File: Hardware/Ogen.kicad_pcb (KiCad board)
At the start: 2 copper layers, 22 x 28 mm, 19 parts, among them J1 Input, U1 TLV70019, U2 PMW3360DM-T2QU, U3 SN74LVC1T45DCK, U4 SN74LVC1T45DCK, U5 SN74LVC1T45DCK, U6 SN74LVC1T45DCK, U7 SN74LVC1T45DCK

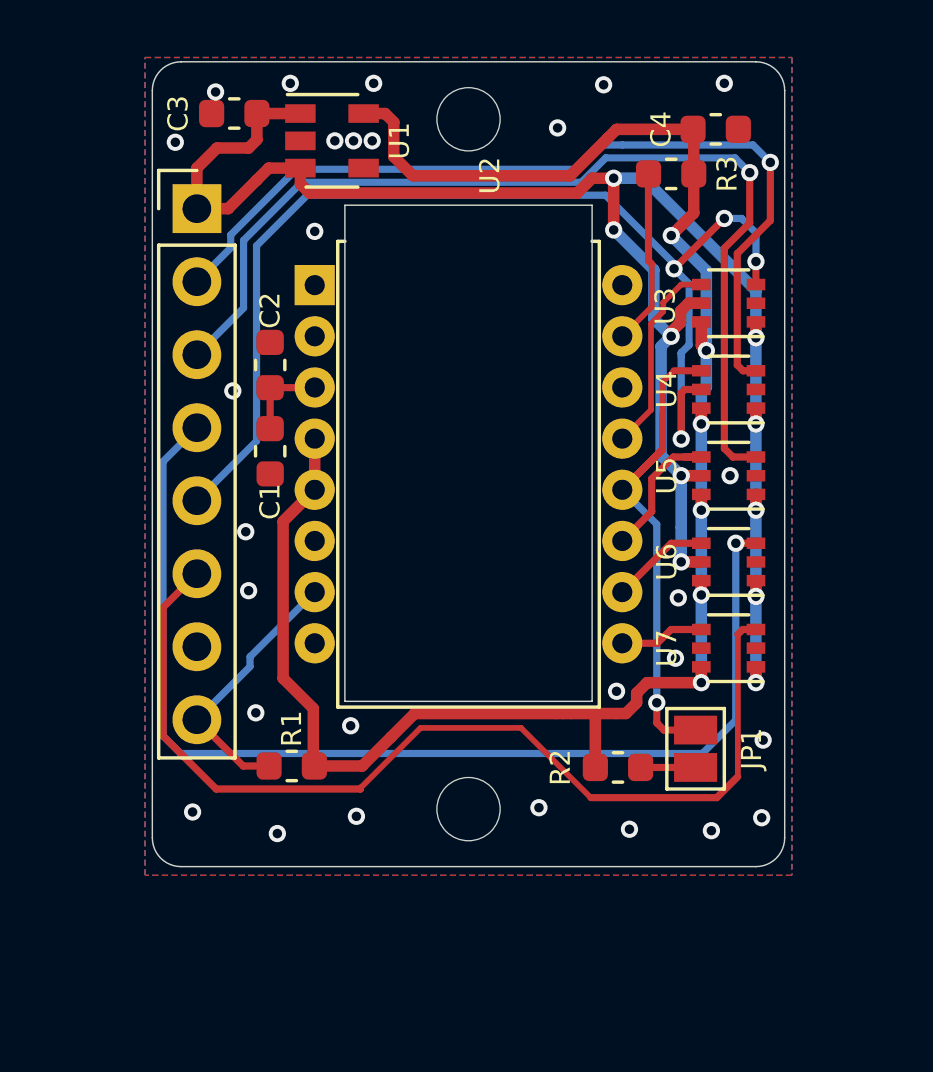
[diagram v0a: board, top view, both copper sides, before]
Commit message: Fixed traces
Some traces weren't the right width so I fixed that. ALso did some minor rerouting.
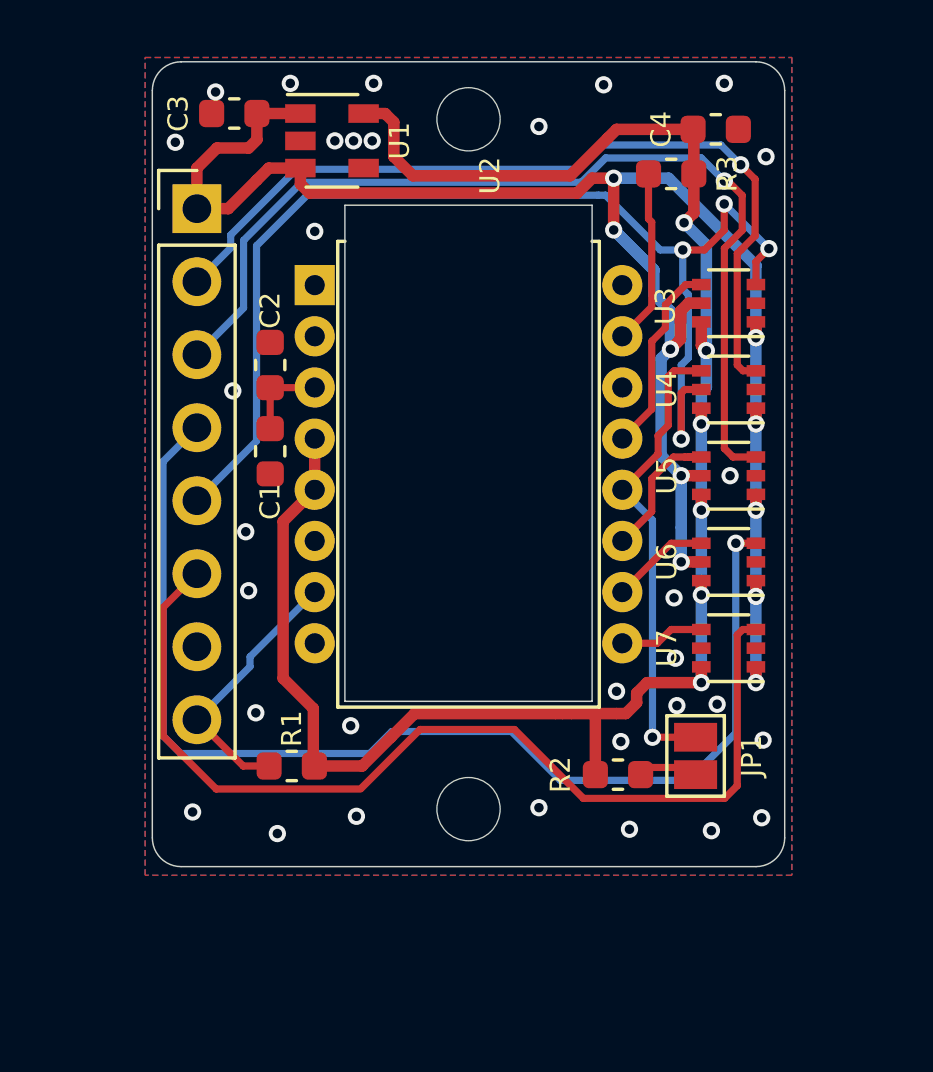
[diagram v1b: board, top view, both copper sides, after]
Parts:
- moved JP1 0.25 mm to (42.9, 35.1)
- moved R2 0.25 mm to (40.2, 35.8)
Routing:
- net VCC: track 63.1 -> 66.5 mm
- net MISO: track 19.1 -> 16.4 mm
- net SCLK-H: track 38.7 -> 40.4 mm
- net MISO-H: track 30.7 -> 29.6 mm
- net SS-H: track 40.5 -> 41.5 mm
- net MOSI-H: track 34.8 -> 34.0 mm
- net GND: vias 28 -> 32

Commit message: Added images and updated readme
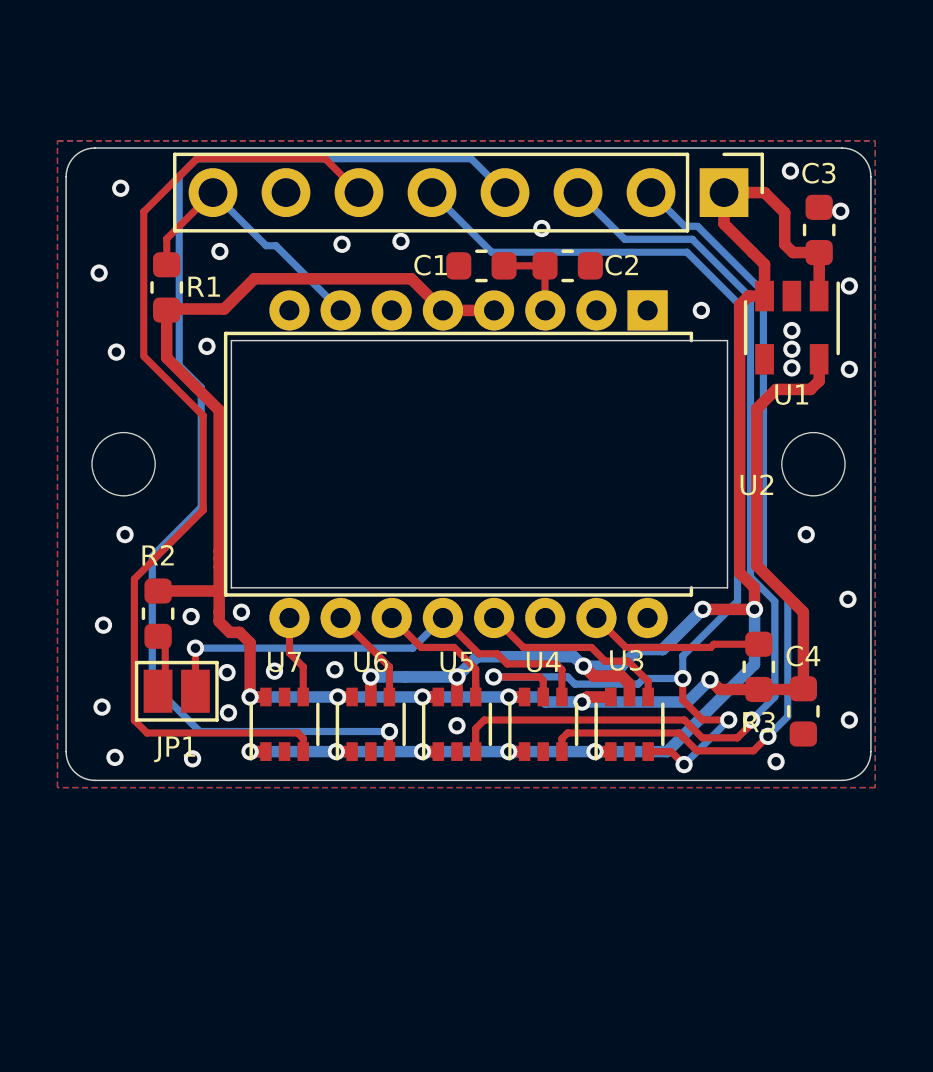
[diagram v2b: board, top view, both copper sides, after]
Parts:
- moved C3 20.7 mm to (47.2, 16.9), turned to 90 degrees
- moved C4 20.5 mm to (46.6, 33.6), turned to 270 degrees
- moved JP1 18.2 mm to (24.9, 32.9), turned to 0 degrees
- moved G*** 17.8 mm to (24.1, 31.2), turned to 180 degrees
- moved R3 17.4 mm to (45.1, 32.0), turned to 90 degrees
- moved U1 17.3 mm to (46.2, 20.2), turned to 270 degrees
- moved R1 17.2 mm to (24.5, 18.9), turned to 270 degrees
- moved REF** 17.0 mm to (47.0, 25.0), turned to 270 degrees
- moved REF** 17.0 mm to (23.0, 25.0), turned to 270 degrees
- moved R2 17.0 mm to (24.2, 30.2), turned to 90 degrees
- moved U7 15.7 mm to (28.6, 34.0), turned to 90 degrees
- moved U3 15.1 mm to (40.6, 34.0), turned to 90 degrees
- moved U6 13.7 mm to (31.6, 34.0), turned to 90 degrees
- moved J1 13.4 mm to (35.0, 15.6), turned to 270 degrees
- moved U4 13.3 mm to (37.6, 34.0), turned to 90 degrees
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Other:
- board size 22 x 28 mm -> 28 x 22 mm

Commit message: Fixed major flaw in PMW3360 footprint
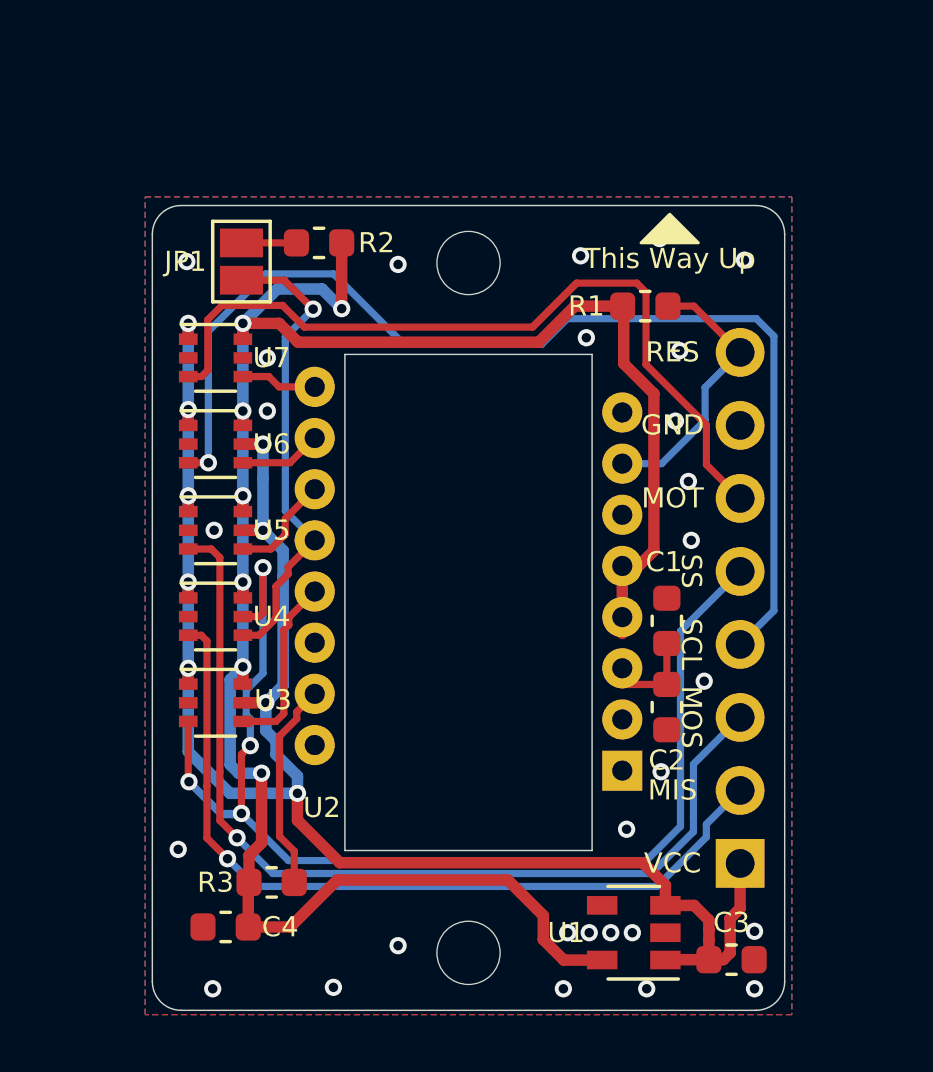
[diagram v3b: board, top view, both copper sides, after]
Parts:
- moved C3 25.6 mm to (44.2, 42.2), turned to 0 degrees
- moved U1 21.8 mm to (40.8, 41.3), turned to 180 degrees
- moved C4 21.5 mm to (26.6, 41.1), turned to 180 degrees
- moved REF** 20.8 mm to (35.0, 42.0), turned to 180 degrees
- moved R3 18.5 mm to (28.1, 39.6), turned to 0 degrees
- moved J1 17.3 mm to (44.5, 30.0), turned to 180 degrees
- moved R1 16.7 mm to (41.1, 19.5), turned to 180 degrees
- moved C2 15.7 mm to (41.9, 33.5), turned to 270 degrees
- moved JP1 15.1 mm to (27.1, 18.0), turned to 270 degrees
- moved U3 14.4 mm to (26.2, 33.3), turned to 0 degrees
- moved R2 14.1 mm to (29.8, 17.3), turned to 0 degrees
- moved C1 13.9 mm to (41.9, 30.4), turned to 90 degrees
- moved REF** 13.9 mm to (35.0, 18.0), turned to 180 degrees
- moved U7 13.0 mm to (26.2, 21.3), turned to 0 degrees
- moved U4 12.0 mm to (26.2, 30.3), turned to 0 degrees
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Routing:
- net VDD: track 65.8 -> 72.5 mm, vias 6 -> 7
- net MOT-H: track 34.8 -> 29.7 mm
- net VCC: track 66.5 -> 61.5 mm, vias 10 -> 9
- net SS-H: track 41.5 -> 44.0 mm
- net SCLK-H: track 40.4 -> 38.6 mm
- net MOSI-H: track 34.0 -> 32.9 mm
- net MISO-H: track 29.6 -> 28.5 mm
- net Net-(R3-Pad2): track 6.17 -> 7.28 mm
- net MOSI: track 5.09 -> 4.26 mm
- net MISO: track 16.4 -> 17.0 mm
- net SCLK: track 3.45 -> 2.86 mm
- net SS: track 6.82 -> 6.23 mm
- net GND: vias 32 -> 28
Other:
- board size 28 x 22 mm -> 22 x 28 mm
- board text added: "GND"
- board text added: "MIS"
- board text added: "MOS"
- board text added: "MOT"
- board text added: "Ogen PMW3360DM-T2QU SPI Breakout Board V1.0 Designed by Aria"
- board text added: "RES"
- board text added: "SCL"
- board text added: "SS"
- board text added: "This Way Up"
- board text added: "VCC"
- board text removed: "Ogen PMW3360 SPI Breakout Board V1.0 Designed by Aria"

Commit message: Updated silk, better render
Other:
- board text added: "Ogen V1.0Aria"
- board text removed: "Ogen PMW3360DM-T2QU SPI Breakout Board V1.0 Designed by Aria"
